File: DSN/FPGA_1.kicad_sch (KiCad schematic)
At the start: 133 parts

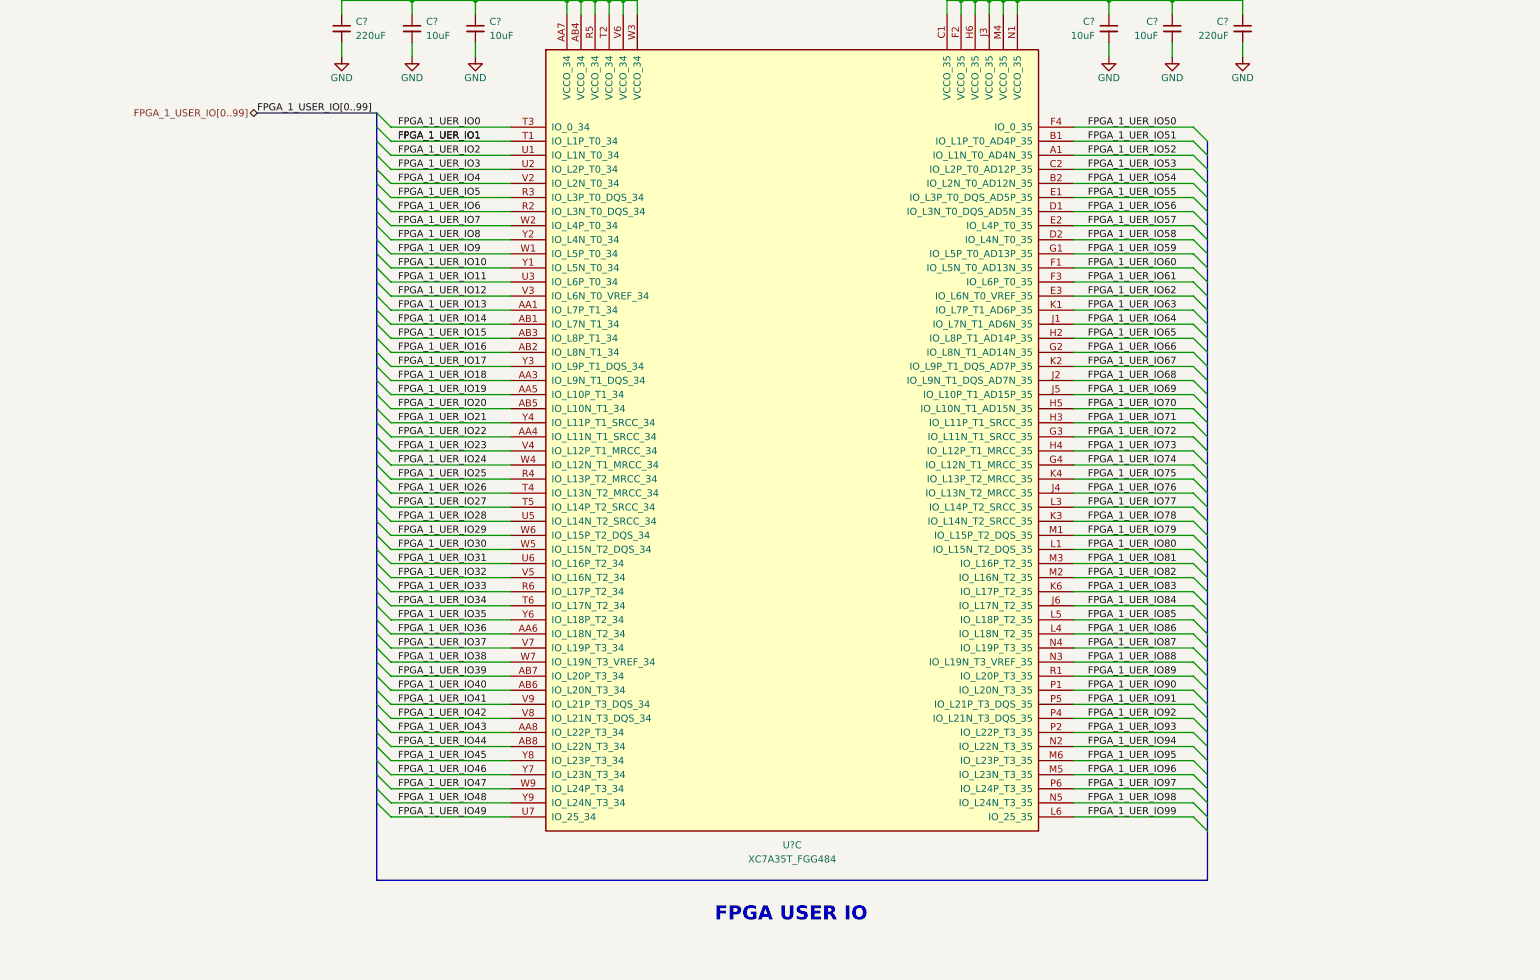
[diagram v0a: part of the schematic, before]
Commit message: Updates
Changed FPGA user io from 100 to 50 per chip, added 4 pmod per FPGA, added 8x buttons + led's, added SMA connectors for FPGA0 GTP.
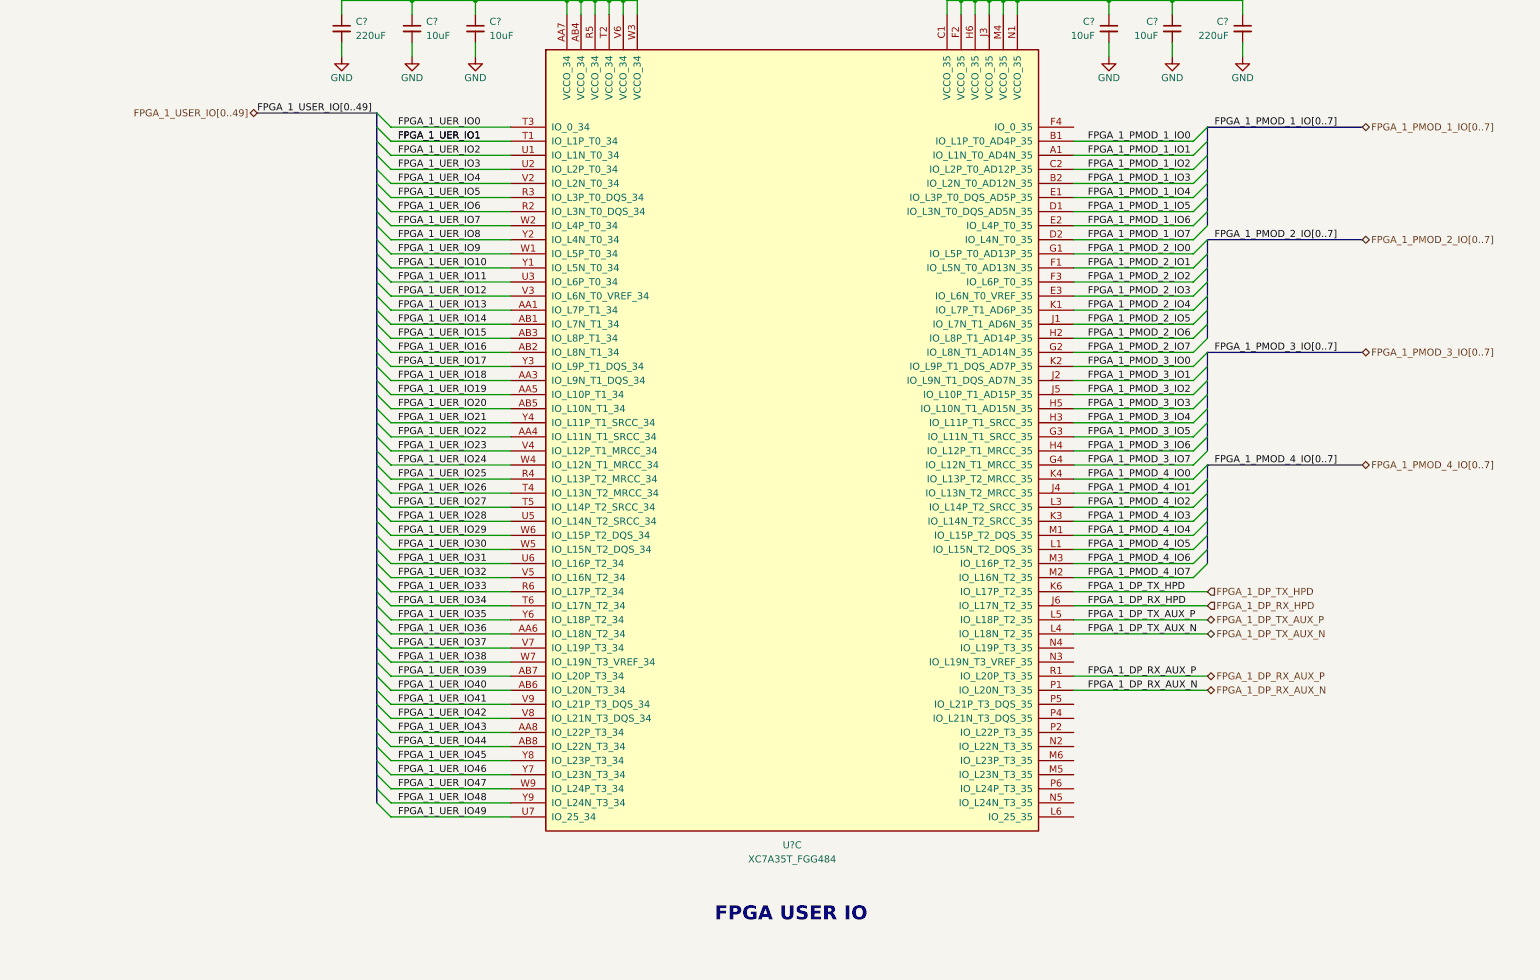
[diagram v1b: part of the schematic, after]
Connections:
- net FPGA_1_UER_IO50: no longer names the net of U?.F4 (IO_0_35)
- net FPGA_1_UER_IO51 renamed FPGA_1_PMOD_1_IO0
- net FPGA_1_UER_IO52 renamed FPGA_1_PMOD_1_IO1
- net FPGA_1_UER_IO53 renamed FPGA_1_PMOD_1_IO2
- net FPGA_1_UER_IO54 renamed FPGA_1_PMOD_1_IO3
- net FPGA_1_UER_IO55 renamed FPGA_1_PMOD_1_IO4
- net FPGA_1_UER_IO56 renamed FPGA_1_PMOD_1_IO5
- net FPGA_1_UER_IO57 renamed FPGA_1_PMOD_1_IO6
- net FPGA_1_UER_IO58 renamed FPGA_1_PMOD_1_IO7
- net FPGA_1_UER_IO59 renamed FPGA_1_PMOD_2_IO0
- net FPGA_1_UER_IO60 renamed FPGA_1_PMOD_2_IO1
- net FPGA_1_UER_IO61 renamed FPGA_1_PMOD_2_IO2
- net FPGA_1_UER_IO62 renamed FPGA_1_PMOD_2_IO3
- net FPGA_1_UER_IO63 renamed FPGA_1_PMOD_2_IO4
- net FPGA_1_UER_IO64 renamed FPGA_1_PMOD_2_IO5
- net FPGA_1_UER_IO65 renamed FPGA_1_PMOD_2_IO6
- net FPGA_1_UER_IO66 renamed FPGA_1_PMOD_2_IO7
- net FPGA_1_UER_IO67 renamed FPGA_1_PMOD_3_IO0
- net FPGA_1_UER_IO68 renamed FPGA_1_PMOD_3_IO1
- net FPGA_1_UER_IO69 renamed FPGA_1_PMOD_3_IO2
- net FPGA_1_UER_IO70 renamed FPGA_1_PMOD_3_IO3
- net FPGA_1_UER_IO71 renamed FPGA_1_PMOD_3_IO4
- net FPGA_1_UER_IO72 renamed FPGA_1_PMOD_3_IO5
- net FPGA_1_UER_IO73 renamed FPGA_1_PMOD_3_IO6
- net FPGA_1_UER_IO74 renamed FPGA_1_PMOD_3_IO7
- net FPGA_1_UER_IO75 renamed FPGA_1_PMOD_4_IO0
- net FPGA_1_UER_IO76 renamed FPGA_1_PMOD_4_IO1
- net FPGA_1_UER_IO77 renamed FPGA_1_PMOD_4_IO2
- net FPGA_1_UER_IO78 renamed FPGA_1_PMOD_4_IO3
- net FPGA_1_UER_IO79 renamed FPGA_1_PMOD_4_IO4
- net FPGA_1_UER_IO80 renamed FPGA_1_PMOD_4_IO5
- net FPGA_1_UER_IO81 renamed FPGA_1_PMOD_4_IO6
- net FPGA_1_UER_IO82 renamed FPGA_1_PMOD_4_IO7
- net FPGA_1_UER_IO83 renamed FPGA_1_DP_TX_HPD
- net FPGA_1_UER_IO84 renamed FPGA_1_DP_RX_HPD
- net FPGA_1_UER_IO85 renamed FPGA_1_DP_TX_AUX_P
- net FPGA_1_UER_IO86 renamed FPGA_1_DP_TX_AUX_N
- net FPGA_1_UER_IO87: no longer names the net of U?.N4 (IO_L19P_T3_35)
- net FPGA_1_UER_IO88: no longer names the net of U?.N3 (IO_L19N_T3_VREF_35)
- net FPGA_1_UER_IO89 renamed FPGA_1_DP_RX_AUX_P
- net FPGA_1_UER_IO90 renamed FPGA_1_DP_RX_AUX_N
- net FPGA_1_UER_IO91: no longer names the net of U?.P5 (IO_L21P_T3_DQS_35)
- net FPGA_1_UER_IO92: no longer names the net of U?.P4 (IO_L21N_T3_DQS_35)
- net FPGA_1_UER_IO93: no longer names the net of U?.P2 (IO_L22P_T3_35)
- net FPGA_1_UER_IO94: no longer names the net of U?.N2 (IO_L22N_T3_35)
- net FPGA_1_UER_IO95: no longer names the net of U?.M6 (IO_L23P_T3_35)
- net FPGA_1_UER_IO96: no longer names the net of U?.M5 (IO_L23N_T3_35)
- net FPGA_1_UER_IO97: no longer names the net of U?.P6 (IO_L24P_T3_35)
- net FPGA_1_UER_IO98: no longer names the net of U?.N5 (IO_L24N_T3_35)
- net FPGA_1_UER_IO99: no longer names the net of U?.L6 (IO_25_35)

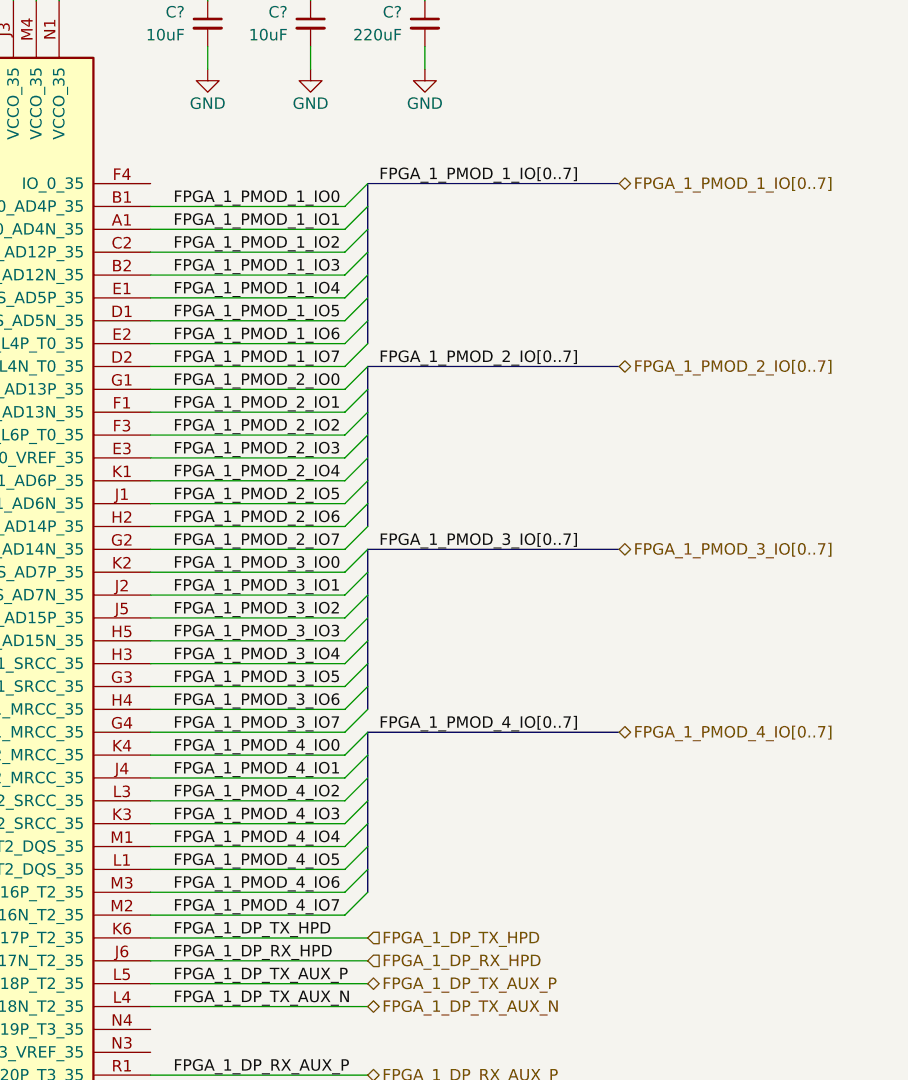
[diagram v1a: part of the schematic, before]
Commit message: Added PSRAM, Finished Schematic
Footprint assignment required, some minor changes to be made to schematic. Sheet naming and commenting to be done.
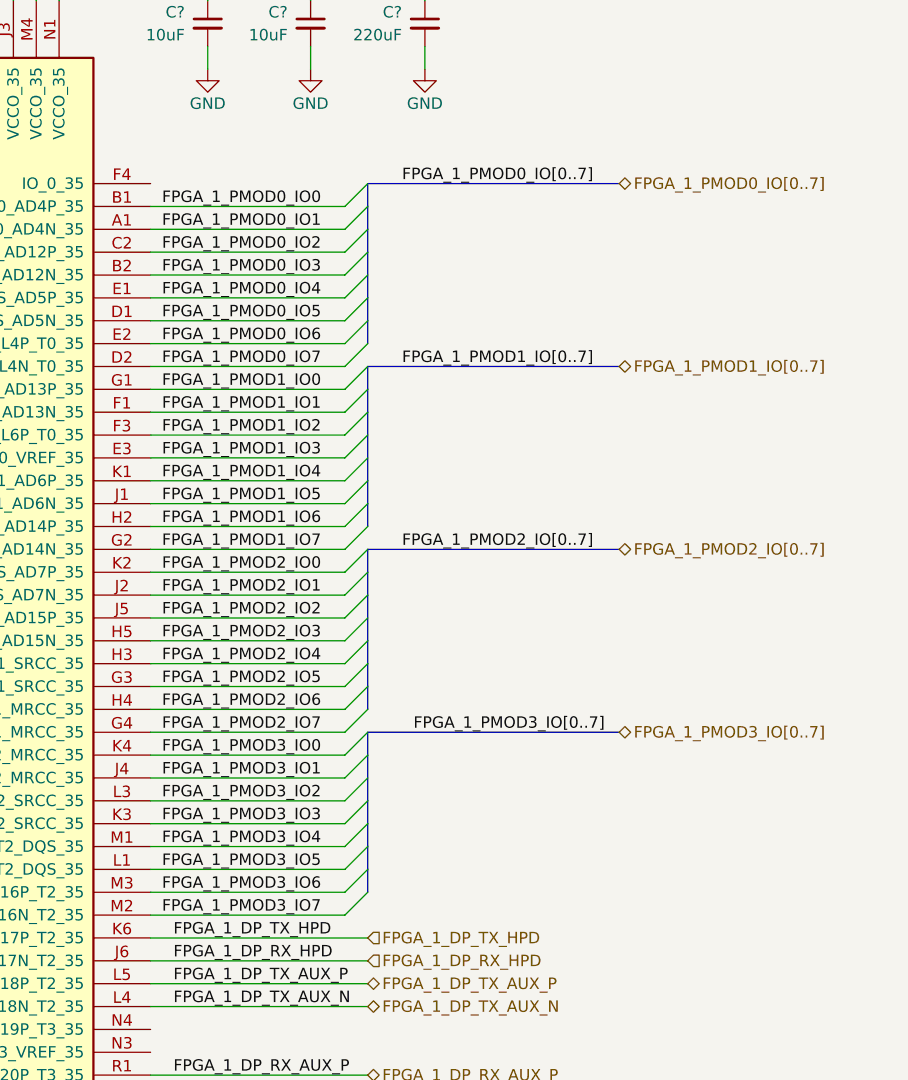
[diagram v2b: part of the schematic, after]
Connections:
- net FPGA_1_PMOD_1_IO0 renamed FPGA_1_PMOD0_IO0
- net FPGA_1_PMOD_1_IO1 renamed FPGA_1_PMOD0_IO1
- net FPGA_1_PMOD_1_IO2 renamed FPGA_1_PMOD0_IO2
- net FPGA_1_PMOD_1_IO3 renamed FPGA_1_PMOD0_IO3
- net FPGA_1_PMOD_1_IO4 renamed FPGA_1_PMOD0_IO4
- net FPGA_1_PMOD_1_IO5 renamed FPGA_1_PMOD0_IO5
- net FPGA_1_PMOD_1_IO6 renamed FPGA_1_PMOD0_IO6
- net FPGA_1_PMOD_1_IO7 renamed FPGA_1_PMOD0_IO7
- net FPGA_1_PMOD_2_IO0 renamed FPGA_1_PMOD1_IO0
- net FPGA_1_PMOD_2_IO1 renamed FPGA_1_PMOD1_IO1
- net FPGA_1_PMOD_2_IO2 renamed FPGA_1_PMOD1_IO2
- net FPGA_1_PMOD_2_IO3 renamed FPGA_1_PMOD1_IO3
- net FPGA_1_PMOD_2_IO4 renamed FPGA_1_PMOD1_IO4
- net FPGA_1_PMOD_2_IO5 renamed FPGA_1_PMOD1_IO5
- net FPGA_1_PMOD_2_IO6 renamed FPGA_1_PMOD1_IO6
- net FPGA_1_PMOD_2_IO7 renamed FPGA_1_PMOD1_IO7
- net FPGA_1_PMOD_3_IO0 renamed FPGA_1_PMOD2_IO0
- net FPGA_1_PMOD_3_IO1 renamed FPGA_1_PMOD2_IO1
- net FPGA_1_PMOD_3_IO2 renamed FPGA_1_PMOD2_IO2
- net FPGA_1_PMOD_3_IO3 renamed FPGA_1_PMOD2_IO3
- net FPGA_1_PMOD_3_IO4 renamed FPGA_1_PMOD2_IO4
- net FPGA_1_PMOD_3_IO5 renamed FPGA_1_PMOD2_IO5
- net FPGA_1_PMOD_3_IO6 renamed FPGA_1_PMOD2_IO6
- net FPGA_1_PMOD_3_IO7 renamed FPGA_1_PMOD2_IO7
- net FPGA_1_PMOD_4_IO0 renamed FPGA_1_PMOD3_IO0
- net FPGA_1_PMOD_4_IO1 renamed FPGA_1_PMOD3_IO1
- net FPGA_1_PMOD_4_IO2 renamed FPGA_1_PMOD3_IO2
- net FPGA_1_PMOD_4_IO3 renamed FPGA_1_PMOD3_IO3
- net FPGA_1_PMOD_4_IO4 renamed FPGA_1_PMOD3_IO4
- net FPGA_1_PMOD_4_IO5 renamed FPGA_1_PMOD3_IO5
- net FPGA_1_PMOD_4_IO6 renamed FPGA_1_PMOD3_IO6
- net FPGA_1_PMOD_4_IO7 renamed FPGA_1_PMOD3_IO7

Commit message: Added Footprints
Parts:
- removed SW?: SW_Push, symbol Switch:SW_Push
- added SW?: SW_Push, Button_Switch_SMD:SW_Push_1P1T_NO_CK_KMR2, symbol Switch:SW_Push
- SW?: footprint (none) -> Button_Switch_SMD:SW_DIP_SPSTx03_Slide_9.78x9.8mm_W8.61mm_P2.54mm
- SW?: footprint (none) -> Button_Switch_SMD:SW_Push_1P1T_NO_CK_KMR2
- U?: footprint (none) -> Package_BGA:Xilinx_FGG484
- U?: footprint (none) -> Package_SO:SOIC-8_3.9x4.9mm_P1.27mm; MFR PN (none) -> IS25LP128F-JBLA3
- U?: footprint (none) -> Oscillator:Oscillator_SMD_SiTime_SiT9121-6Pin_3.2x2.5mm
- U?: footprint (none) -> Package_DFN_QFN:VDFN-6
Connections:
- net FPGA_1_SYSRST: now also SW?.1
- net GND: now also SW?.2
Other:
- title: (none) -> FPGA 1
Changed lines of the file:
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@@
 (kicad_sch (version 20211123) (generator eeschema)
   (paper "A1")
+  (title_block
+    (title "FPGA 1")
+    (date "2023-03-07")
+    (rev "A")
+    (comment 1 "Designed by DragonEnjoyer :3")
+  )
   (junction (at 115.57 420.37) (diameter 0) (color 0 0 0 0)
   )
@@
     (property "Reference" "SW?" (id 0) (at 683.26 438.15 0))
     (property "Value" "SW_DIP_x03" (id 1) (at 683.26 440.69 0))
-    (property "Footprint" "" (id 2) (at 683.26 450.85 0)
+    (property "Footprint" "Button_Switch_SMD:SW_DIP_SPSTx03_Slide_9.78x9.8mm_W8.61mm_P2.54mm" (id 2) (at 683.26 450.85 0)
       (effects (font (size 1.27 1.27)) hide)
     )
@@
       (effects (font (size 1.27 1.27)) (justify right))
     )
-    (property "Footprint" "" (id 2) (at 190.5 133.35 0)
+    (property "Footprint" "Package_BGA:Xilinx_FGG484" (id 2) (at 190.5 133.35 0)
       (effects (font (size 1.27 1.27)) hide)
     )
@@
     (property "Reference" "SW?" (id 0) (at 736.6 431.8 0))
     (property "Value" "SW_Push" (id 1) (at 736.6 434.34 0))
-    (property "Footprint" "" (id 2) (at 736.6 434.34 0)
+    (property "Footprint" "Button_Switch_SMD:SW_Push_1P1T_NO_CK_KMR2" (id 2) (at 736.6 434.34 0)
       (effects (font (size 1.27 1.27)) hide)
     )
@@
     (property "Reference" "U?" (id 0) (at 641.35 508 0))
     (property "Value" "IS25LP128F" (id 1) (at 641.35 510.54 0))
-    (property "Footprint" "" (id 2) (at 627.38 530.86 0)
+    (property "Footprint" "Package_SO:SOIC-8_3.9x4.9mm_P1.27mm" (id 2) (at 627.38 530.86 0)
+      (effects (font (size 1.27 1.27)) hide)
+    )
+    (property "Datasheet" "https://www.issi.com/WW/pdf/25LP-WP128F.pdf" (id 3) (at 627.38 530.86 0)
       (effects (font (size 1.27 1.27)) hide)
     )
-    (property "Datasheet" "" (id 3) (at 627.38 530.86 0)
+    (property "MFR PN" "IS25LP128F-JBLA3" (id 4) (at 627.38 530.86 0)
       (effects (font (size 1.27 1.27)) hide)
     )
@@
     (pin "2")
   )
+  (symbol (lib_id "Switch:SW_Push") (at 736.6 454.66 0) (unit 1)
+    (in_bom yes) (on_board yes) (fields_autoplaced)
+    (property "Reference" "SW?" (id 0) (at 736.6 447.04 0))
+    (property "Value" "SW_Push" (id 1) (at 736.6 449.58 0))
+    (property "Footprint" "Button_Switch_SMD:SW_Push_1P1T_NO_CK_KMR2" (id 2) (at 736.6 449.58 0)
+      (effects (font (size 1.27 1.27)) hide)
+    )
+    (property "Datasheet" "~" (id 3) (at 736.6 449.58 0)
+      (effects (font (size 1.27 1.27)) hide)
+    )
+    (pin "1")
+    (pin "2")
+  )
   (symbol (lib_id "power:GND") (at 72.39 372.11 0) (unit 1)
     (in_bom yes) (on_board yes)
@@
     (property "Reference" "U?" (id 0) (at 200.025 223.52 0))
     (property "Value" "SIT9120AI" (id 1) (at 200.025 226.06 0))
-    (property "Footprint" "" (id 2) (at 167.64 233.68 0)
+    (property "Footprint" "Oscillator:Oscillator_SMD_SiTime_SiT9121-6Pin_3.2x2.5mm" (id 2) (at 167.64 233.68 0)
       (effects (font (size 1.27 1.27)) hide)
     )
-    (property "Datasheet" "" (id 3) (at 167.64 233.68 0)
+    (property "Datasheet" "https://www.sitime.com/datasheet/SiT9120" (id 3) (at 167.64 233.68 0)
       (effects (font (size 1.27 1.27)) hide)
     )
@@
     (property "Reference" "U?" (id 0) (at 437.515 439.42 0))
     (property "Value" "DSC1103BI2-135.0000" (id 1) (at 437.515 441.96 0))
-    (property "Footprint" "" (id 2) (at 411.48 447.04 0)
+    (property "Footprint" "Package_DFN_QFN:VDFN-6" (id 2) (at 411.48 447.04 0)
       (effects (font (size 1.27 1.27)) hide)
     )
-    (property "Datasheet" "" (id 3) (at 411.48 447.04 0)
+    (property "Datasheet" "https://rocelec.widen.net/view/pdf/9j4mxdnz0b/MCHP-S-A0006612827-1.pdf?t.download=true&u=5oefqw" (id 3) (at 411.48 447.04 0)
       (effects (font (size 1.27 1.27)) hide)
     )
@@
     (pin "1")
   )
-  (symbol (lib_id "Switch:SW_Push") (at 736.6 454.66 0) (unit 1)
-    (in_bom yes) (on_board yes) (fields_autoplaced)
-    (property "Reference" "SW?" (id 0) (at 736.6 447.04 0))
-    (property "Value" "SW_Push" (id 1) (at 736.6 449.58 0))
-    (property "Footprint" "" (id 2) (at 736.6 449.58 0)
-      (effects (font (size 1.27 1.27)) hide)
-    )
-    (property "Datasheet" "~" (id 3) (at 736.6 449.58 0)
-      (effects (font (size 1.27 1.27)) hide)
-    )
-    (pin "1")
-    (pin "2")
-  )
   (symbol (lib_id "power:GND") (at 304.8 372.11 0) (unit 1)

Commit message: Added component ref des
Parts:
- added C355: 100nF, Capacitor_SMD:C_0402_1005Metric, symbol Device:C_Small
- added U30: TC1047AVNBTR, digikey-footprints:SOT-23-3, symbol dk_Temperature-Sensors-Analog-and-Digital-Output:TC1047AVNBTR
- gave numbers to parts that had none: 127
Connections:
- net +1V8: now also U10.K10 (VCCADC_0)
- net +3V3: now also C355.1, U30.1 (VDD)
- net GND: now also U10.K9 (GNDADC_0), C355.2, U30.3 (GND)
- new net TSNS_FPGA1: U30.2 (VOUT)

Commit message: Fixed all ERC Errors
Warnings can be ignored
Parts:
- added C201: 100nF, Capacitor_SMD:C_0402_1005Metric, symbol Device:C_Small
- added TP11, TP12: TestPoint_Probe, TestPoint:TestPoint_Loop_D2.50mm_Drill1.85mm, symbol Connector:TestPoint_Probe
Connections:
- net FPGA_PROGB is gone; now on net FPGA_1_PROGB: R62.1
- net FPGA_1_GTP_CLK_C_P: now also C201.1
- net FPGA_1_GTP_CLK_P: now also C201.2
- net FPGA_1_VREF_P: now also TP12.1
- net TSNS_FPGA1: now also TP11.1
- net FPGA_1_UER_IO0 renamed FPGA_1_USER_IO0
- net FPGA_1_UER_IO1 renamed FPGA_1_USER_IO1
- net FPGA_1_UER_IO10 renamed FPGA_1_USER_IO10
- net FPGA_1_UER_IO11 renamed FPGA_1_USER_IO11
- net FPGA_1_UER_IO12 renamed FPGA_1_USER_IO12
- net FPGA_1_UER_IO13 renamed FPGA_1_USER_IO13
- net FPGA_1_UER_IO14 renamed FPGA_1_USER_IO14
- net FPGA_1_UER_IO15 renamed FPGA_1_USER_IO15
- net FPGA_1_UER_IO16 renamed FPGA_1_USER_IO16
- net FPGA_1_UER_IO17 renamed FPGA_1_USER_IO17
- net FPGA_1_UER_IO18 renamed FPGA_1_USER_IO18
- net FPGA_1_UER_IO19 renamed FPGA_1_USER_IO19
- net FPGA_1_UER_IO2 renamed FPGA_1_USER_IO2
- net FPGA_1_UER_IO20 renamed FPGA_1_USER_IO20
- net FPGA_1_UER_IO21 renamed FPGA_1_USER_IO21
- net FPGA_1_UER_IO22 renamed FPGA_1_USER_IO22
- net FPGA_1_UER_IO23 renamed FPGA_1_USER_IO23
- net FPGA_1_UER_IO24 renamed FPGA_1_USER_IO24
- net FPGA_1_UER_IO25 renamed FPGA_1_USER_IO25
- net FPGA_1_UER_IO26 renamed FPGA_1_USER_IO26
- net FPGA_1_UER_IO27 renamed FPGA_1_USER_IO27
- net FPGA_1_UER_IO28 renamed FPGA_1_USER_IO28
- net FPGA_1_UER_IO29 renamed FPGA_1_USER_IO29
- net FPGA_1_UER_IO3 renamed FPGA_1_USER_IO3
- net FPGA_1_UER_IO30 renamed FPGA_1_USER_IO30
- net FPGA_1_UER_IO31 renamed FPGA_1_USER_IO31
- net FPGA_1_UER_IO32 renamed FPGA_1_USER_IO32
- net FPGA_1_UER_IO33 renamed FPGA_1_USER_IO33
- net FPGA_1_UER_IO34 renamed FPGA_1_USER_IO34
- net FPGA_1_UER_IO35 renamed FPGA_1_USER_IO35
- net FPGA_1_UER_IO36 renamed FPGA_1_USER_IO36
- net FPGA_1_UER_IO37 renamed FPGA_1_USER_IO37
- net FPGA_1_UER_IO38 renamed FPGA_1_USER_IO38
- net FPGA_1_UER_IO39 renamed FPGA_1_USER_IO39
- net FPGA_1_UER_IO4 renamed FPGA_1_USER_IO4
- net FPGA_1_UER_IO40 renamed FPGA_1_USER_IO40
- net FPGA_1_UER_IO41 renamed FPGA_1_USER_IO41
- net FPGA_1_UER_IO42 renamed FPGA_1_USER_IO42
- net FPGA_1_UER_IO43 renamed FPGA_1_USER_IO43
- net FPGA_1_UER_IO44 renamed FPGA_1_USER_IO44
- net FPGA_1_UER_IO45 renamed FPGA_1_USER_IO45
- net FPGA_1_UER_IO46 renamed FPGA_1_USER_IO46
- net FPGA_1_UER_IO47 renamed FPGA_1_USER_IO47
- net FPGA_1_UER_IO48 renamed FPGA_1_USER_IO48
- net FPGA_1_UER_IO49 renamed FPGA_1_USER_IO49
- net FPGA_1_UER_IO5 renamed FPGA_1_USER_IO5
- net FPGA_1_UER_IO6 renamed FPGA_1_USER_IO6
- net FPGA_1_UER_IO7 renamed FPGA_1_USER_IO7
- net FPGA_1_UER_IO8 renamed FPGA_1_USER_IO8
- net FPGA_1_UER_IO9 renamed FPGA_1_USER_IO9
- no-connect marks 4 -> 17
